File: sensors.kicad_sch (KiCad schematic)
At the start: 97 parts, among them M1 CD74HC4067SM, M2 CD74HC4067SM, M3 CD74HC4067SM, M4 CD74HC4067SM, M5 CD74HC4067SM, M6 CD74HC4067SM

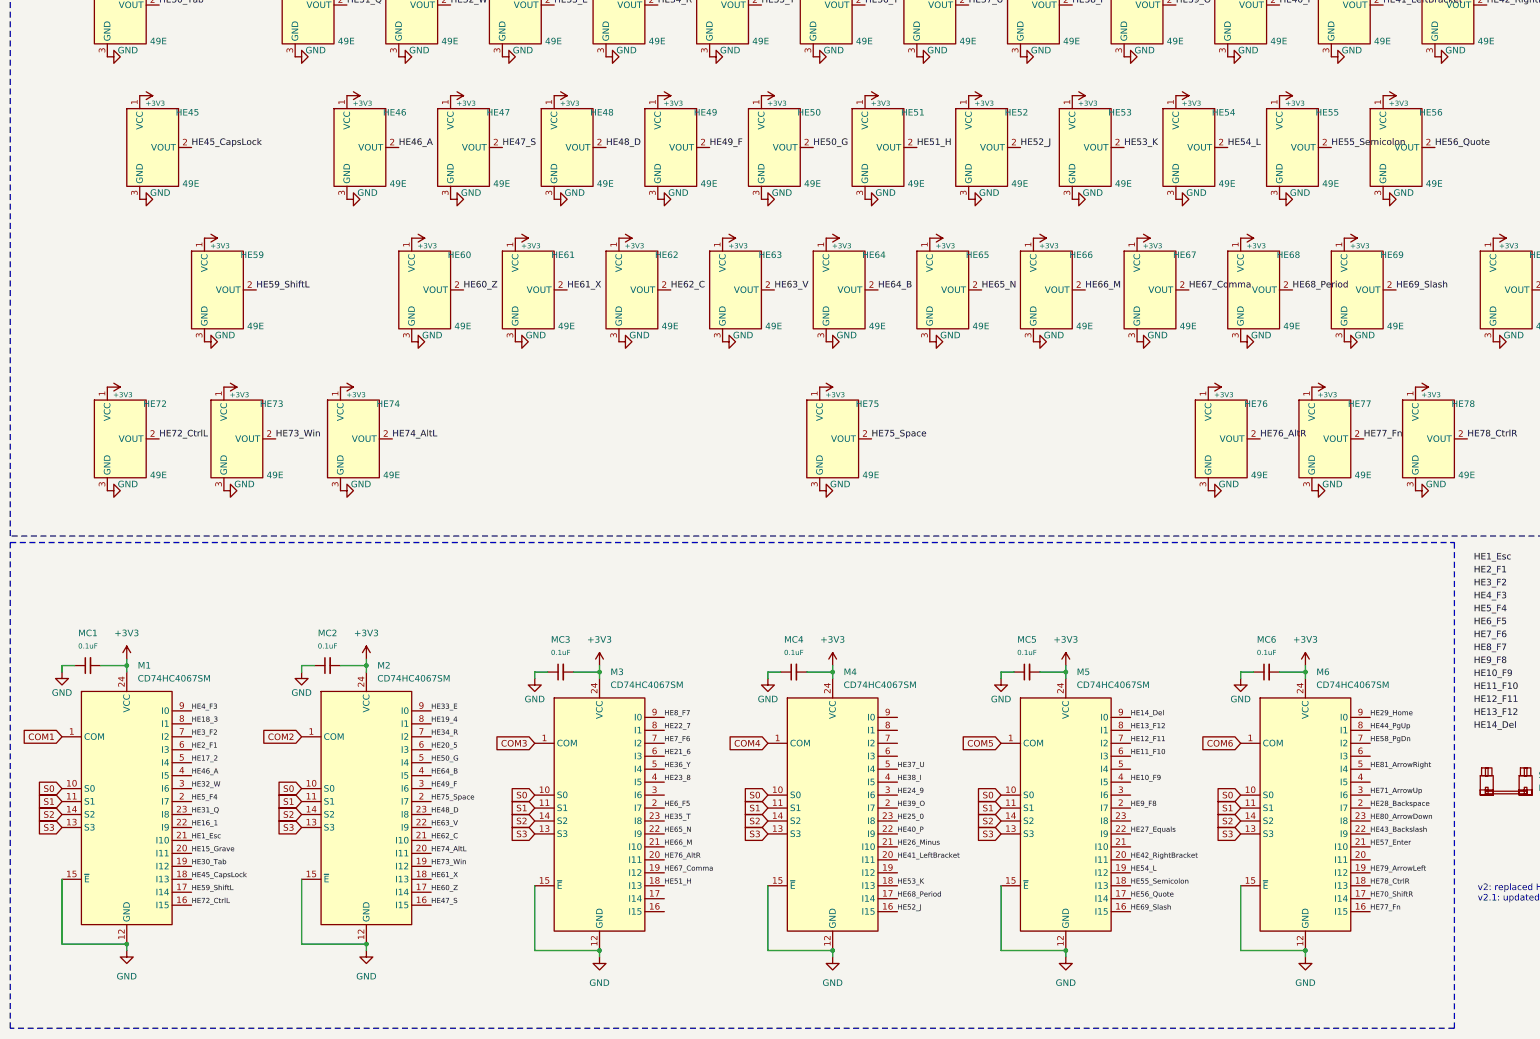
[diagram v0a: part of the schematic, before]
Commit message: Rev 2: Major PCB rework — haptic motor, MicroSD, NTC, CTP, split spacebar
- Added ERM haptic motor with BSS138 MOSFET driver on GP21
- Added MicroSD card slot (MSD-1-A, push-in/auto-eject)
- Added NTC thermistor with voltage divider
- Added 4-pin 0.5mm FPC connector for capacitive touch panel
- Added ferrite beads (0603 600R, 0805) for power filtering
- Added 1N4148WT protection diode and test point
- Split spacebar support: HE45 alternate 1.75u stabilizer footprint
- Full PCB re-route with 4-layer switch footprints
- All 81 hall sensors relabeled with key names in schematic
- Relaxed DRC (text height, via diameter), new via size 0.6/0.2
- Added CHANGELOG.md and wiring.cpp MUX mapping reference
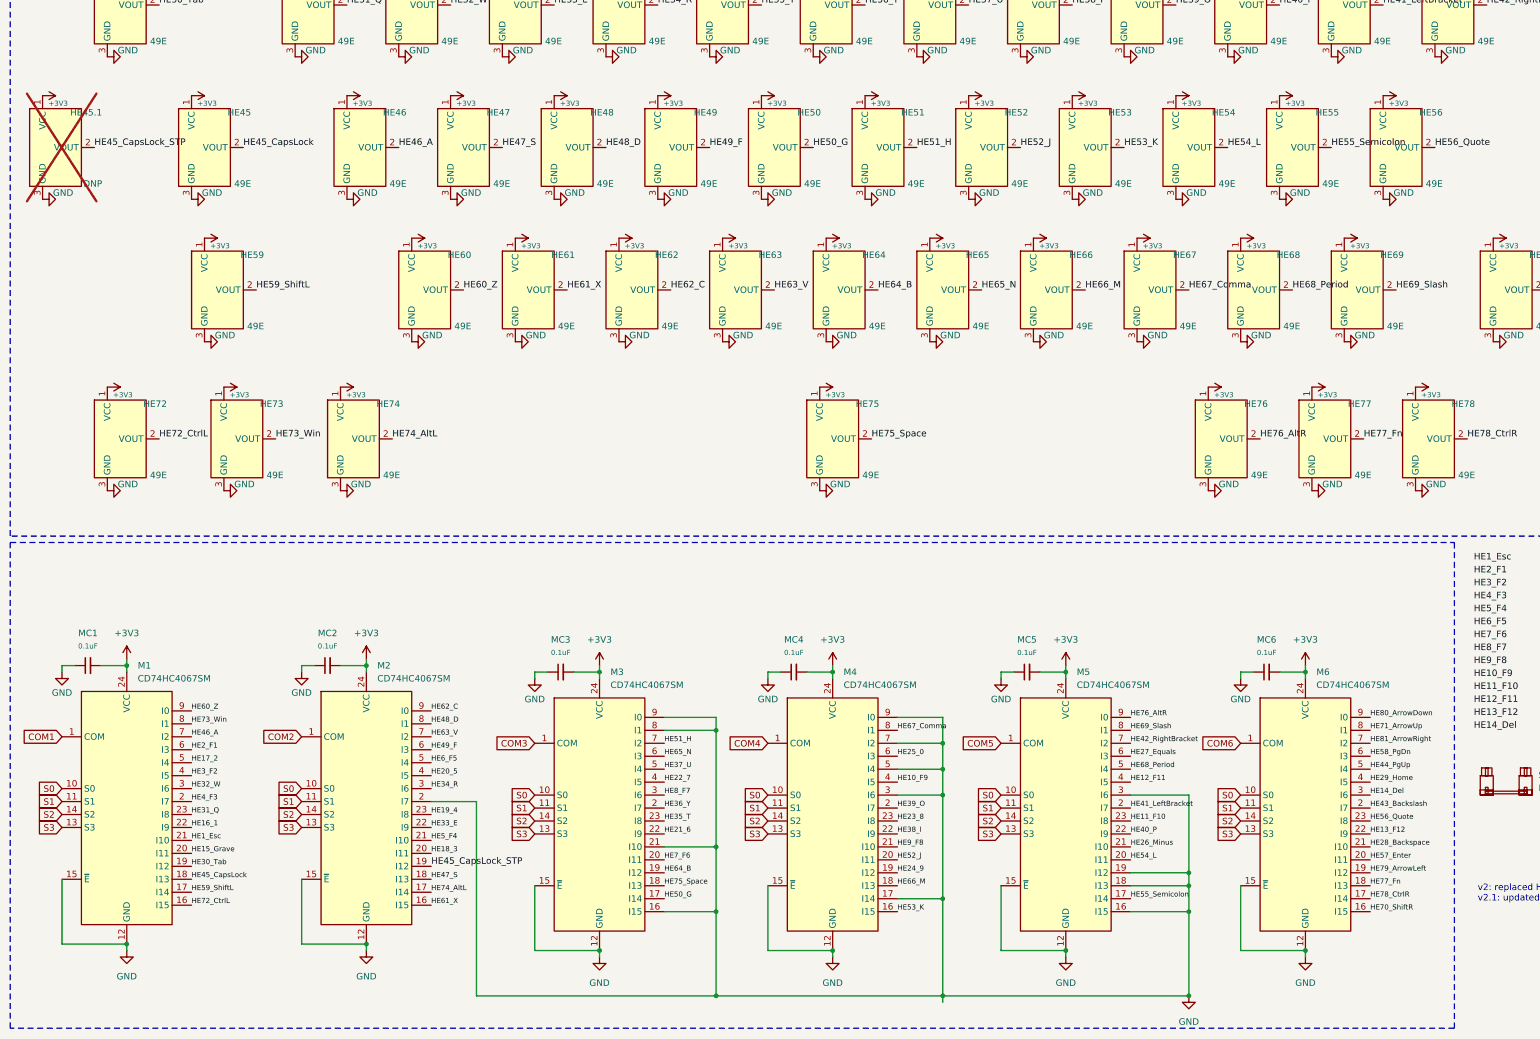
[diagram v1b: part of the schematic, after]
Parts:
- added HE45.1: DNP, PCM_marbastlib-xp-he:SW_MX_HE_90deg_1.75u_STP_1.5_4layer, symbol PCM_marbastlib-he:SW_MX_HE
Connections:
- net +3V3: now also HE45.1.1 (VCC)
- net GND: now also M2.2 (I7), M3.16 (I15), M3.21 (I10), M3.8 (I1), M3.9 (I0), M4.17 (I14), M4.3 (I6), M4.5 (I4), M4.7 (I2), M4.9 (I0), M5.16 (I15), M5.18 (I13), M5.19 (I12), M5.3 (I6), HE45.1.3 (GND)
- net HE10_F9: now also M4.4 (I5); no longer M5.4 (I5)
- net HE11_F10: now also M5.23 (I8); no longer M5.6 (I3)
- net HE12_F11: now also M5.4 (I5); no longer M5.7 (I2)
- net HE13_F12: now also M6.22 (I9); no longer M5.8 (I1)
- net HE14_Del: now also M6.3 (I6); no longer M5.9 (I0)
- net HE18_3: now also M2.20 (I11); no longer M1.8 (I1)
- net HE19_4: now also M2.23 (I8); no longer M2.8 (I1)
- net HE20_5: now also M2.4 (I5); no longer M2.6 (I3)
- net HE21_6: now also M3.22 (I9); no longer M3.6 (I3)
- net HE22_7: now also M3.4 (I5); no longer M3.8 (I1)
- net HE23_8: now also M4.23 (I8); no longer M3.4 (I5)
- net HE24_9: now also M4.19 (I12); no longer M4.3 (I6)
- net HE25_0: now also M4.6 (I3); no longer M4.23 (I8)
- net HE26_Minus: now also M5.21 (I10); no longer M4.21 (I10)
- net HE27_Equals: now also M5.6 (I3); no longer M5.22 (I9)
- net HE28_Backspace: now also M6.21 (I10); no longer M6.2 (I7)
- net HE29_Home: now also M6.4 (I5); no longer M6.9 (I0)
- net HE33_E: now also M2.22 (I9); no longer M2.9 (I0)
- net HE34_R: now also M2.3 (I6); no longer M2.7 (I2)
- net HE36_Y: now also M3.2 (I7); no longer M3.5 (I4)
- net HE37_U: now also M3.5 (I4); no longer M4.5 (I4)
- net HE38_I: now also M4.22 (I9); no longer M4.4 (I5)
- net HE3_F2: now also M1.4 (I5); no longer M1.7 (I2)
- net HE40_P: now also M5.22 (I9); no longer M4.22 (I9)
- net HE41_LeftBracket: now also M5.2 (I7); no longer M4.20 (I11)
- net HE42_RightBracket: now also M5.7 (I2); no longer M5.20 (I11)
- net HE43_Backslash: now also M6.2 (I7); no longer M6.22 (I9)
- net HE44_PgUp: now also M6.5 (I4); no longer M6.8 (I1)
- net HE46_A: now also M1.7 (I2); no longer M1.4 (I5)
- net HE47_S: now also M2.18 (I13); no longer M2.16 (I15)
- net HE48_D: now also M2.8 (I1); no longer M2.23 (I8)
- net HE49_F: now also M2.6 (I3); no longer M2.3 (I6)
- net HE4_F3: now also M1.2 (I7); no longer M1.9 (I0)
- net HE50_G: now also M3.17 (I14); no longer M2.5 (I4)
- net HE51_H: now also M3.7 (I2); no longer M3.18 (I13)
- net HE52_J: now also M4.20 (I11); no longer M4.16 (I15)
- net HE53_K: now also M4.16 (I15); no longer M4.18 (I13)
- net HE54_L: now also M5.20 (I11); no longer M5.19 (I12)
- net HE55_Semicolon: now also M5.17 (I14); no longer M5.18 (I13)
- net HE56_Quote: now also M6.23 (I8); no longer M5.17 (I14)
- net HE57_Enter: now also M6.20 (I11); no longer M6.21 (I10)
- net HE58_PgDn: now also M6.6 (I3); no longer M6.7 (I2)
- net HE5_F4: now also M2.21 (I10); no longer M1.2 (I7)
- net HE60_Z: now also M1.9 (I0); no longer M2.17 (I14)
- net HE61_X: now also M2.16 (I15); no longer M2.18 (I13)
- net HE62_C: now also M2.9 (I0); no longer M2.21 (I10)
- net HE63_V: now also M2.7 (I2); no longer M2.22 (I9)
- net HE64_B: now also M3.19 (I12); no longer M2.4 (I5)
- net HE65_N: now also M3.6 (I3); no longer M3.22 (I9)
- net HE66_M: now also M4.18 (I13); no longer M3.21 (I10)
- net HE67_Comma: now also M4.8 (I1); no longer M3.19 (I12)
- net HE68_Period: now also M5.5 (I4); no longer M4.17 (I14)
- net HE69_Slash: now also M5.8 (I1); no longer M5.16 (I15)
- net HE6_F5: now also M2.5 (I4); no longer M3.2 (I7)
- net HE70_ShiftR: now also M6.16 (I15); no longer M6.17 (I14)
- net HE71_ArrowUp: now also M6.8 (I1); no longer M6.3 (I6)
- net HE73_Win: now also M1.8 (I1); no longer M2.19 (I12)
- net HE74_AltL: now also M2.17 (I14); no longer M2.20 (I11)
- net HE75_Space: now also M3.18 (I13); no longer M2.2 (I7)
- net HE76_AltR: now also M5.9 (I0); no longer M3.20 (I11)
- net HE77_Fn: now also M6.18 (I13); no longer M6.16 (I15)
- net HE78_CtrlR: now also M6.17 (I14); no longer M6.18 (I13)
- net HE7_F6: now also M3.20 (I11); no longer M3.7 (I2)
- net HE80_ArrowDown: now also M6.9 (I0); no longer M6.23 (I8)
- net HE81_ArrowRight: now also M6.7 (I2); no longer M6.5 (I4)
- net HE8_F7: now also M3.3 (I6); no longer M3.9 (I0)
- net HE9_F8: now also M4.21 (I10); no longer M5.2 (I7)
- new net HE45_CapsLock_STP: HE45.1.2 (VOUT), M2.19 (I12)
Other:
- moved on the sheet: HE45

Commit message: VLT_rev1 PCB complete — production files added
Finalized schematic and PCB layout. Added production/ with
Gerbers (VLT_rev1.zip), BOM, pick-and-place positions, and
IPC netlist for fabrication.
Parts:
- S28: footprint PCM_marbastlib-mx:STAB_MX_P_2u -> PCM_marbastlib-mx:STAB_MX_2u
- S57, S59: footprint PCM_marbastlib-mx:STAB_MX_P_2.25u -> PCM_marbastlib-mx:STAB_MX_2.25u
- S75: footprint PCM_marbastlib-mx:STAB_MX_P_6.25u -> PCM_marbastlib-mx:STAB_MX_6.25u
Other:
- note removed: "v2: replaced HC4067 with ADG732 muxes v2.1: updated +3.3V to +3V3"
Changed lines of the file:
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@@
 		)
 	)
-	(text "v2: replaced HC4067 with ADG732 muxes\nv2.1: updated +3.3V to +3V3"
-		(exclude_from_sim no)
-		(at 301.752 256.794 0)
-		(effects
-			(font
-				(size 1.27 1.27)
-			)
-			(justify left)
-		)
-	)
 	(text "KNOB"
 		(exclude_from_sim no)
@@
 			)
 		)
-		(property "Footprint" "PCM_marbastlib-mx:STAB_MX_P_2.25u"
+		(property "Footprint" "PCM_marbastlib-mx:STAB_MX_2.25u"
 			(at 347.98 234.95 0)
 			(effects
@@
 			)
 		)
-		(property "Footprint" "PCM_marbastlib-mx:STAB_MX_P_2u"
+		(property "Footprint" "PCM_marbastlib-mx:STAB_MX_2u"
 			(at 307.34 234.95 0)
 			(effects
@@
 			)
 		)
-		(property "Footprint" "PCM_marbastlib-mx:STAB_MX_P_2.25u"
+		(property "Footprint" "PCM_marbastlib-mx:STAB_MX_2.25u"
 			(at 327.66 234.95 0)
 			(effects
@@
 			)
 		)
-		(property "Footprint" "PCM_marbastlib-mx:STAB_MX_P_6.25u"
+		(property "Footprint" "PCM_marbastlib-mx:STAB_MX_6.25u"
 			(at 368.3 234.95 0)
 			(effects
